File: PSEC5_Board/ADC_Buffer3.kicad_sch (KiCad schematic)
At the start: 36 parts, among them IC6 LTC6409IUDB#TRMPBF, IC7 LTC6409IUDB#TRMPBF, IC8 LTC6409IUDB#TRMPBF

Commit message: Added Footprints to Schematic
Added footprints to schematic, should be able to now update the layout design and have all nets be present
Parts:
- C66, C67, C69, C71, C74, C75, C76, C77, C78, C79, C80, C81, C82, C83, C84, C85, C86, C87, C88, C89, C90: footprint (none) -> Capacitor_SMD:C_0603_1608Metric
- IC6, IC7, IC8: footprint footprints:QFN-10_UDB_LIT -> LTC6409IUDB_TRMPBF:QFN-10_UDB_LIT
- R42, R43, R44, R45, R46, R47, R48, R49, R50, R51, R52, R53: footprint (none) -> Resistor_SMD:R_0603_1608Metric
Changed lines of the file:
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@@
 			)
 		)
-		(property "Footprint" ""
+		(property "Footprint" "Capacitor_SMD:C_0603_1608Metric"
 			(at 54.61 143.2052 0)
 			(effects
@@
 			)
 		)
-		(property "Footprint" ""
+		(property "Footprint" "Capacitor_SMD:C_0603_1608Metric"
 			(at 265.43 82.8548 0)
 			(effects
@@
 			)
 		)
-		(property "Footprint" ""
+		(property "Footprint" "Capacitor_SMD:C_0603_1608Metric"
 			(at 265.43 71.4248 0)
 			(effects
@@
 			)
 		)
-		(property "Footprint" ""
+		(property "Footprint" "Resistor_SMD:R_0603_1608Metric"
 			(at 59.436 155.194 90)
 			(effects
@@
 			)
 		)
-		(property "Footprint" ""
+		(property "Footprint" "Capacitor_SMD:C_0603_1608Metric"
 			(at 53.34 55.5752 0)
 			(effects
@@
 			)
 		)
-		(property "Footprint" ""
+		(property "Footprint" "Capacitor_SMD:C_0603_1608Metric"
 			(at 171.45 109.5248 0)
 			(effects
@@
 			)
 		)
-		(property "Footprint" ""
+		(property "Footprint" "Capacitor_SMD:C_0603_1608Metric"
 			(at 132.08 30.7848 0)
 			(effects
@@
 			)
 		)
-		(property "Footprint" ""
+		(property "Footprint" "Resistor_SMD:R_0603_1608Metric"
 			(at 35.306 147.066 90)
 			(effects
@@
 			)
 		)
-		(property "Footprint" ""
+		(property "Footprint" "Capacitor_SMD:C_0603_1608Metric"
 			(at 186.69 96.2152 0)
 			(effects
@@
 			)
 		)
-		(property "Footprint" ""
+		(property "Footprint" "Capacitor_SMD:C_0603_1608Metric"
 			(at 132.08 42.2148 0)
 			(effects
@@
 			)
 		)
-		(property "Footprint" ""
+		(property "Footprint" "Capacitor_SMD:C_0603_1608Metric"
 			(at 133.35 118.4148 0)
 			(effects
@@
 			)
 		)
-		(property "Footprint" ""
+		(property "Footprint" "Resistor_SMD:R_0603_1608Metric"
 			(at 55.626 39.116 90)
 			(effects
@@
 			)
 		)
-		(property "Footprint" ""
+		(property "Footprint" "Capacitor_SMD:C_0603_1608Metric"
 			(at 59.69 26.9748 0)
 			(effects
@@
 			)
 		)
-		(property "Footprint" ""
+		(property "Footprint" "Resistor_SMD:R_0603_1608Metric"
 			(at 42.926 42.926 90)
 			(effects
@@
 			)
 		)
-		(property "Footprint" ""
+		(property "Footprint" "Capacitor_SMD:C_0603_1608Metric"
 			(at 132.08 167.9448 0)
 			(effects
@@
 			)
 		)
-		(property "Footprint" ""
+		(property "Footprint" "Capacitor_SMD:C_0603_1608Metric"
 			(at 130.81 80.3148 0)
 			(effects
@@
 			)
 		)
-		(property "Footprint" ""
+		(property "Footprint" "Capacitor_SMD:C_0603_1608Metric"
 			(at 264.16 120.9548 0)
 			(effects
@@
 			)
 		)
-		(property "Footprint" ""
+		(property "Footprint" "Capacitor_SMD:C_0603_1608Metric"
 			(at 60.96 114.6048 0)
 			(effects
@@
 			)
 		)
-		(property "Footprint" ""
+		(property "Footprint" "Capacitor_SMD:C_0603_1608Metric"
 			(at 193.04 67.6148 0)
 			(effects
@@
 			)
 		)
-		(property "Footprint" ""
+		(property "Footprint" "Resistor_SMD:R_0603_1608Metric"
 			(at 176.276 83.566 90)
 			(effects
@@
 			)
 		)
-		(property "Footprint" ""
+		(property "Footprint" "Resistor_SMD:R_0603_1608Metric"
 			(at 56.896 126.746 90)
 			(effects
@@
 			)
 		)
-		(property "Footprint" ""
+		(property "Footprint" "Resistor_SMD:R_0603_1608Metric"
 			(at 34.036 59.436 90)
 			(effects
@@
 			)
 		)
-		(property "Footprint" ""
+		(property "Footprint" "Resistor_SMD:R_0603_1608Metric"
 			(at 191.516 108.204 90)
 			(effects
@@
 			)
 		)
-		(property "Footprint" ""
+		(property "Footprint" "Capacitor_SMD:C_0603_1608Metric"
 			(at 264.16 109.5248 0)
 			(effects
@@
 			)
 		)
-		(property "Footprint" ""
+		(property "Footprint" "Resistor_SMD:R_0603_1608Metric"
 			(at 44.196 130.556 90)
 			(effects
@@
 			)
 		)
-		(property "Footprint" ""
+		(property "Footprint" "Resistor_SMD:R_0603_1608Metric"
 			(at 167.386 100.076 90)
 			(effects
@@
 			)
 		)
-		(property "Footprint" ""
+		(property "Footprint" "Capacitor_SMD:C_0603_1608Metric"
 			(at 39.37 156.5148 0)
 			(effects
@@
 			)
 		)
-		(property "Footprint" "footprints:QFN-10_UDB_LIT"
+		(property "Footprint" "LTC6409IUDB_TRMPBF:QFN-10_UDB_LIT"
 			(at 105.41 220.65 0)
 			(effects
@@
 			)
 		)
-		(property "Footprint" ""
+		(property "Footprint" "Capacitor_SMD:C_0603_1608Metric"
 			(at 132.08 156.5148 0)
 			(effects
@@
 			)
 		)
-		(property "Footprint" ""
+		(property "Footprint" "Resistor_SMD:R_0603_1608Metric"
 			(at 58.166 67.564 90)
 			(effects
@@
 			)
 		)
-		(property "Footprint" ""
+		(property "Footprint" "Capacitor_SMD:C_0603_1608Metric"
 			(at 133.35 129.8448 0)
 			(effects
@@
 			)
 		)
-		(property "Footprint" "footprints:QFN-10_UDB_LIT"
+		(property "Footprint" "LTC6409IUDB_TRMPBF:QFN-10_UDB_LIT"
 			(at 104.14 133.02 0)
 			(effects
@@
 			)
 		)
-		(property "Footprint" "footprints:QFN-10_UDB_LIT"
+		(property "Footprint" "LTC6409IUDB_TRMPBF:QFN-10_UDB_LIT"
 			(at 237.49 173.66 0)
 			(effects
@@
 			)
 		)
-		(property "Footprint" ""
+		(property "Footprint" "Resistor_SMD:R_0603_1608Metric"
 			(at 188.976 79.756 90)
 			(effects
@@
 			)
 		)
-		(property "Footprint" ""
+		(property "Footprint" "Capacitor_SMD:C_0603_1608Metric"
 			(at 130.81 68.8848 0)
 			(effects
@@
 			)
 		)
-		(property "Footprint" ""
+		(property "Footprint" "Capacitor_SMD:C_0603_1608Metric"
 			(at 38.1 68.8848 0)
 			(effects

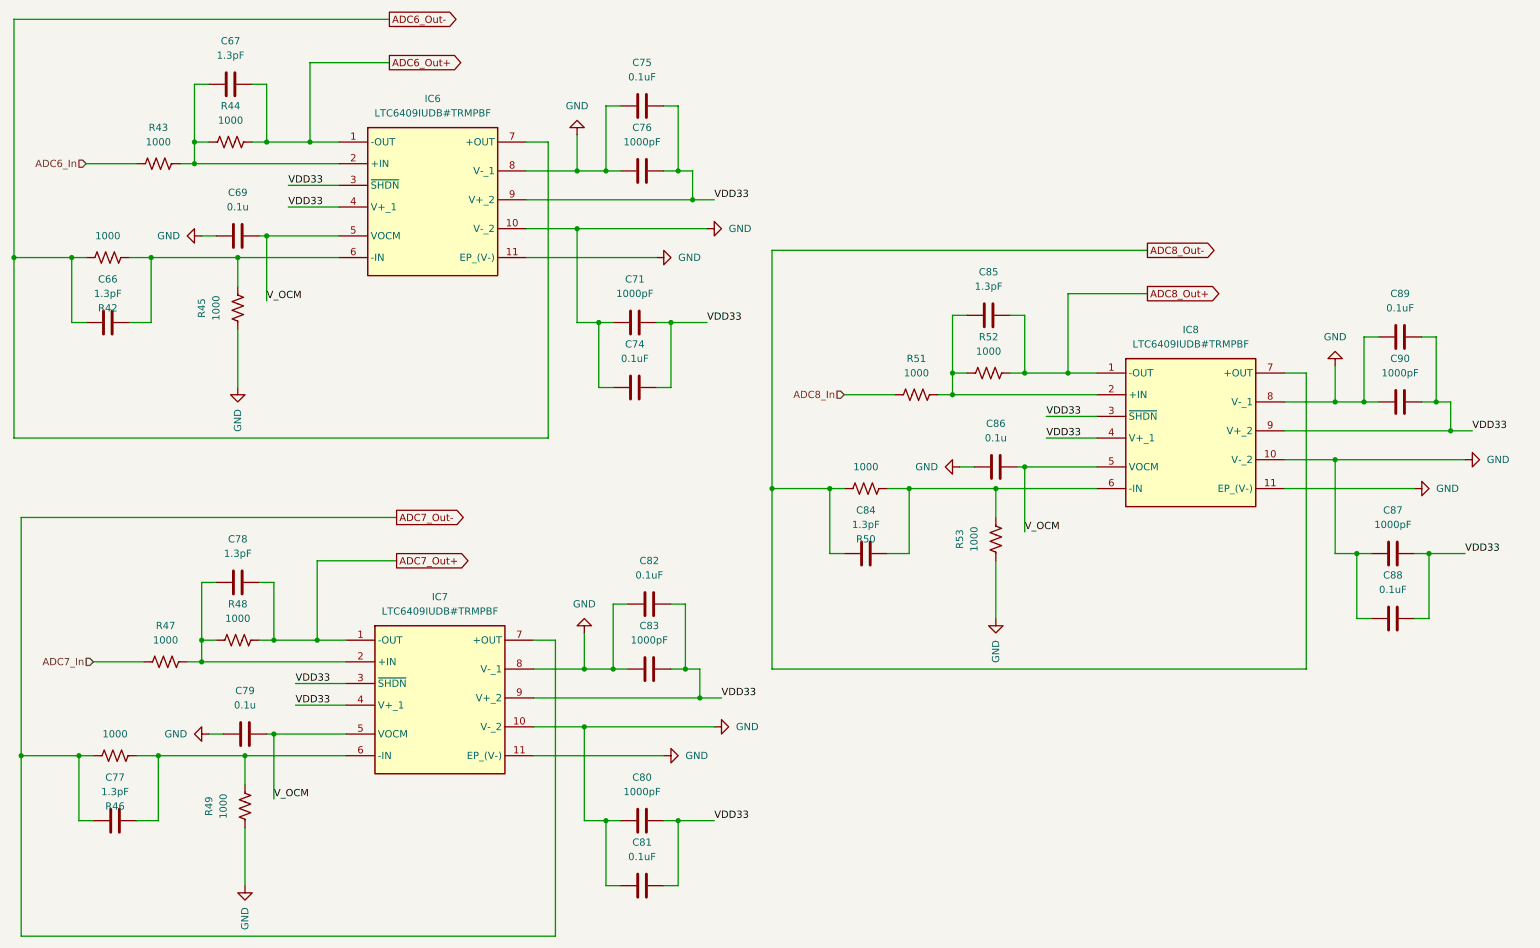
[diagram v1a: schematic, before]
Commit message: DUT Layout Overhaul
Footprints need to be replaced.
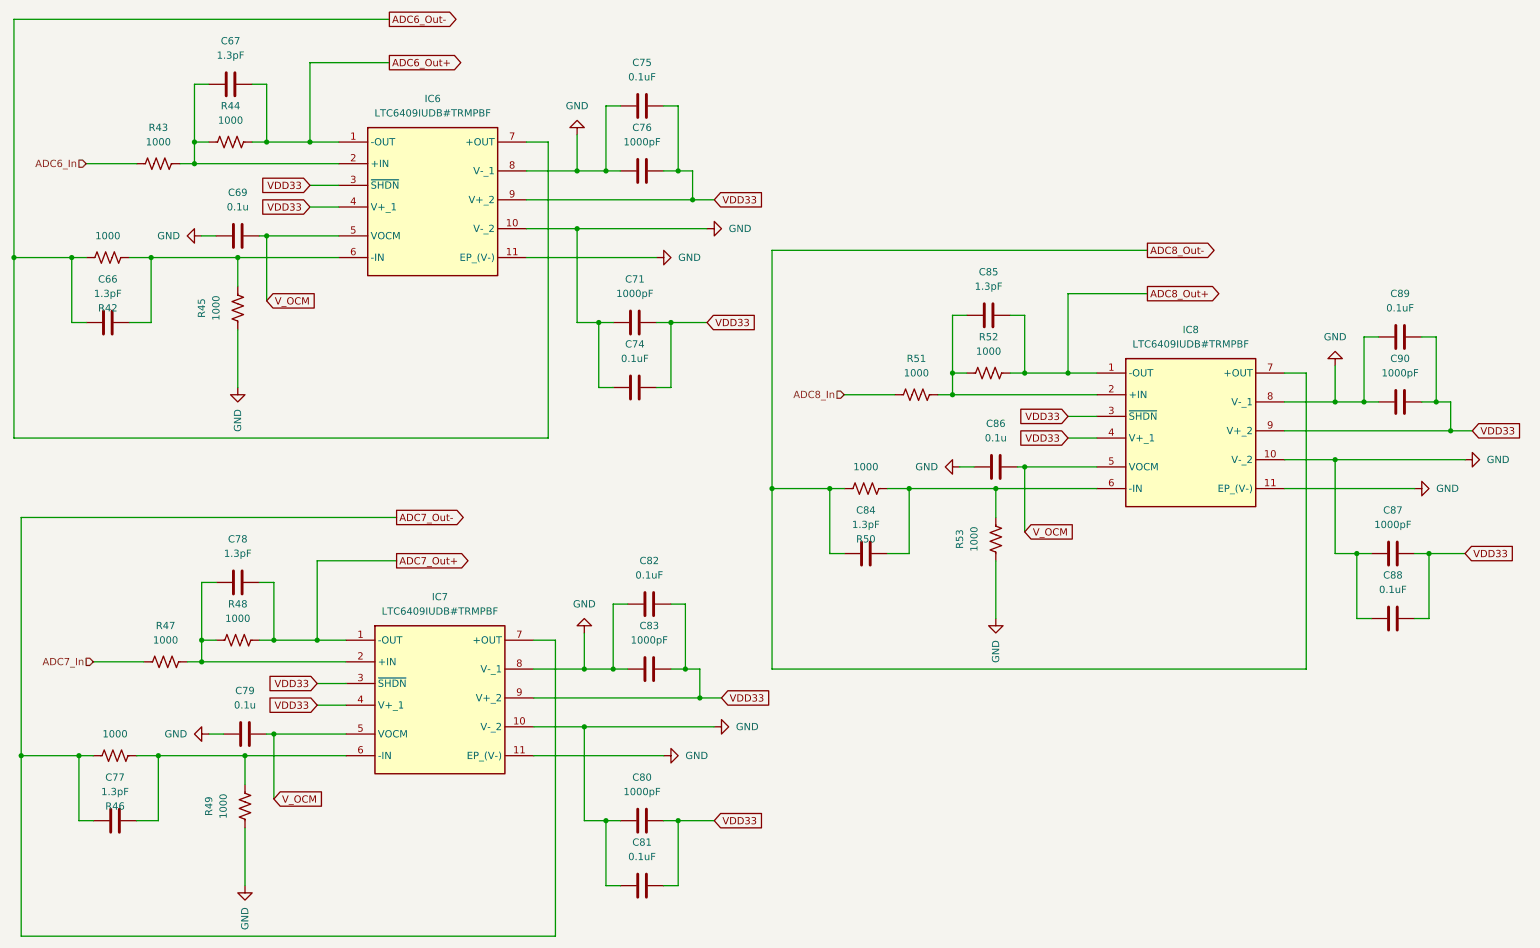
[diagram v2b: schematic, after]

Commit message: DUT v4 Push
Addressed the issues discussed in last week's meeting, cleared ERC errors, still any warnings with Solder Mask.
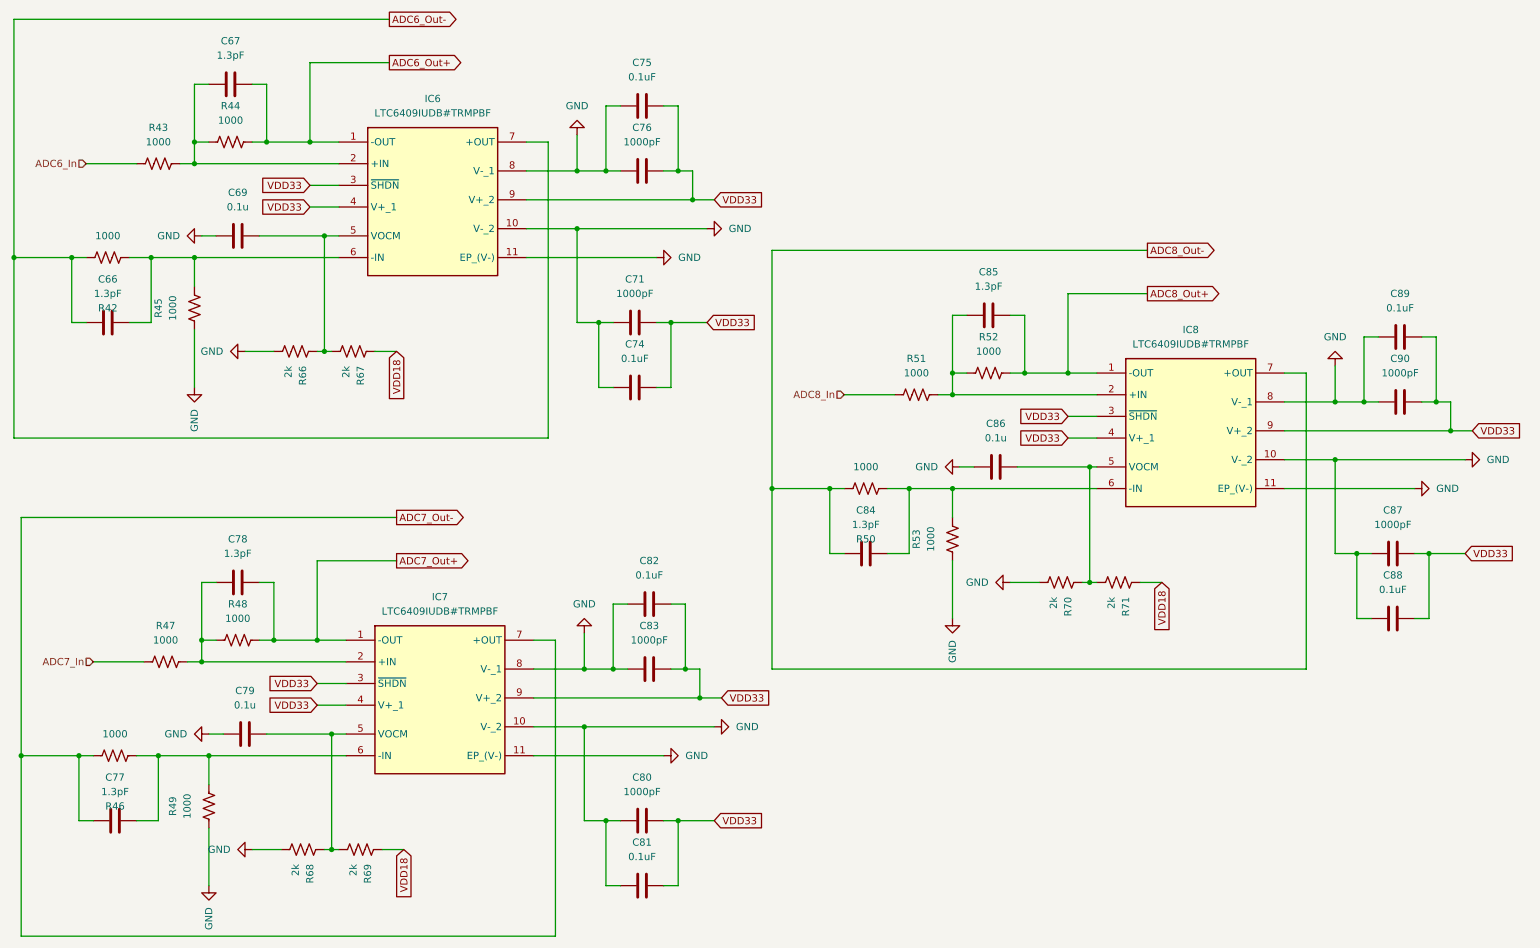
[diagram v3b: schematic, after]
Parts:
- added R66, R67, R68, R69, R70, R71: 2k, Resistor_SMD:R_0603_1608Metric, symbol Device:R_US
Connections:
- net GND: now also R66.2, R68.2, R70.2
- removed net V_OCM: C69.1, C79.1, C86.1, IC6.5 (VOCM), IC7.5 (VOCM), IC8.5 (VOCM)
- new net: C79.1, IC7.5 (VOCM), R68.1, R69.2
- new net: C69.1, IC6.5 (VOCM), R66.1, R67.2
- new net: C86.1, IC8.5 (VOCM), R70.1, R71.2
- new net VDD18: R67.1, R69.1, R71.1
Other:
- moved on the sheet: R45, R49, R53

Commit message: Merge Richmond's production board from JoeModifications into same branch as other boards
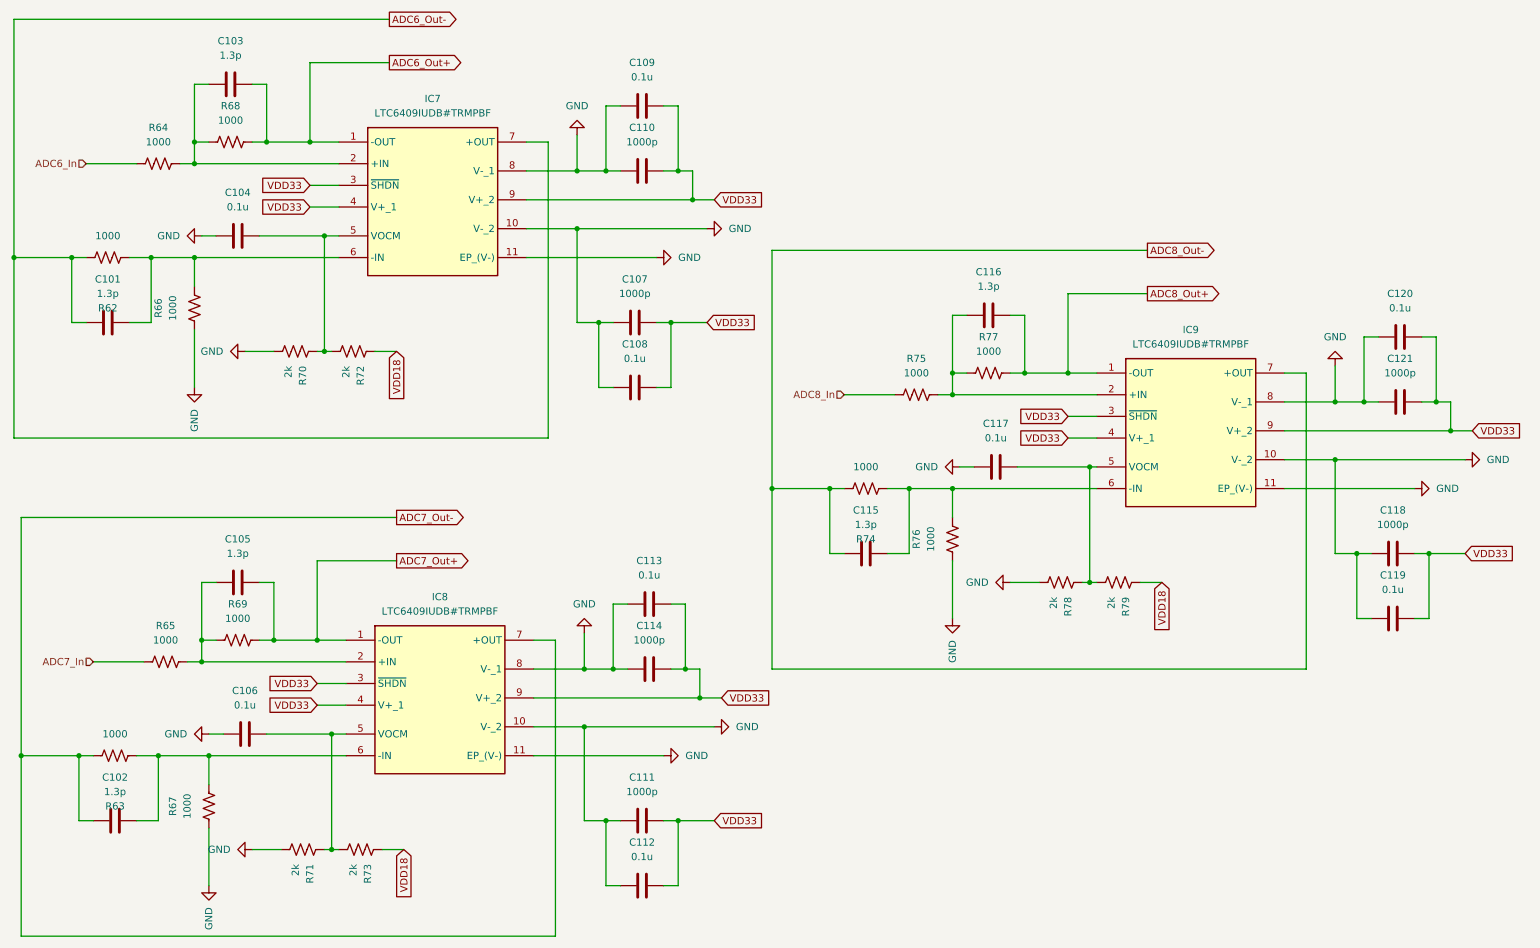
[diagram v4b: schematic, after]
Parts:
- C101: renamed from C66; value 1.3pF -> 1.3p
- C102: renamed from C77; value 1.3pF -> 1.3p
- C103: renamed from C67; value 1.3pF -> 1.3p
- C105: renamed from C78; value 1.3pF -> 1.3p
- C107: renamed from C71; value 1000pF -> 1000p
- C108: renamed from C74; value 0.1uF -> 0.1u
- C109: renamed from C75; value 0.1uF -> 0.1u
- C110: renamed from C76; value 1000pF -> 1000p
- C111: renamed from C80; value 1000pF -> 1000p
- C112: renamed from C81; value 0.1uF -> 0.1u
- C113: renamed from C82; value 0.1uF -> 0.1u
- C114: renamed from C83; value 1000pF -> 1000p
- C115: renamed from C84; value 1.3pF -> 1.3p
- C116: renamed from C85; value 1.3pF -> 1.3p
- C118: renamed from C87; value 1000pF -> 1000p
- C119: renamed from C88; value 0.1uF -> 0.1u
- C120: renamed from C89; value 0.1uF -> 0.1u
- C121: renamed from C90; value 1000pF -> 1000p
- renumbered C69 to C104, C79 to C106, C86 to C117, IC6 to IC7, IC7 to IC8, IC8 to IC9, R42 to R62, R46 to R63, R43 to R64, R47 to R65, R45 to R66, R49 to R67, R44 to R68, R48 to R69, R66 to R70, R68 to R71, R67 to R72, R69 to R73, R50 to R74, R51 to R75, R53 to R76, R52 to R77, R70 to R78, R71 to R79
